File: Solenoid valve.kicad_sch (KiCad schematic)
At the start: 21 parts, among them J2 Conn_01x02, J3 Conn_01x02, J4 Conn_01x02, Q1 S8050, Q2 S8050, U1 BTS443P

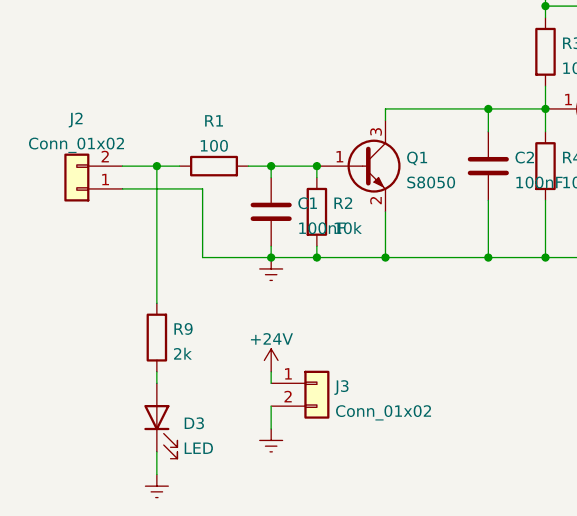
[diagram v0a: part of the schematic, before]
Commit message: Delete a LED
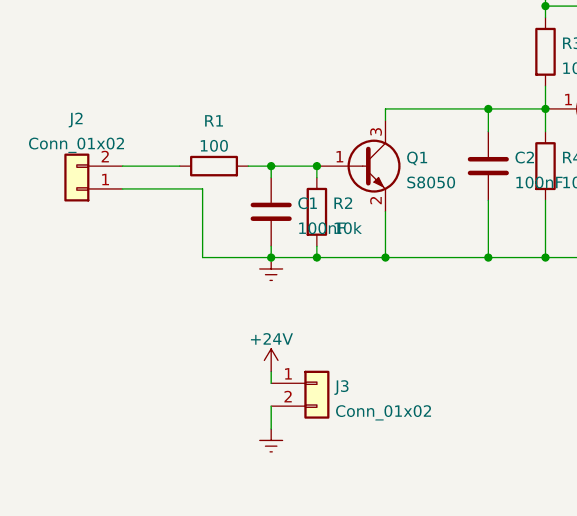
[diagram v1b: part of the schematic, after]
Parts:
- removed D3: LED, LED_SMD:LED_0603_1608Metric_Pad1.05x0.95mm_HandSolder, symbol Device:LED
- removed R9: 2k, Resistor_SMD:R_0603_1608Metric_Pad0.98x0.95mm_HandSolder, symbol Device:R
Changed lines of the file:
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@@
   (junction (at 176.53 66.04) (diameter 0) (color 0 0 0 0)
   )
-  (junction (at 90.17 76.2) (diameter 0) (color 0 0 0 0)
-  )
   (junction (at 127 69.85) (diameter 0) (color 0 0 0 0)
   )
@@
     (stroke (width 0) (type default) (color 0 0 0 0))
   )
-  (wire (pts (xy 86.36 76.2) (xy 90.17 76.2))
+  (wire (pts (xy 86.36 76.2) (xy 92.71 76.2))
     (stroke (width 0) (type default) (color 0 0 0 0))
   )
@@
     (stroke (width 0) (type default) (color 0 0 0 0))
   )
-  (wire (pts (xy 90.17 110.49) (xy 90.17 107.95))
-    (stroke (width 0) (type default) (color 0 0 0 0))
-  )
   (wire (pts (xy 102.87 77.47) (xy 102.87 76.2))
     (stroke (width 0) (type default) (color 0 0 0 0))
@@
     (stroke (width 0) (type default) (color 0 0 0 0))
   )
-  (wire (pts (xy 90.17 76.2) (xy 90.17 91.44))
-    (stroke (width 0) (type default) (color 0 0 0 0))
-  )
   (wire (pts (xy 133.35 86.36) (xy 127 86.36))
     (stroke (width 0) (type default) (color 0 0 0 0))
@@
     (stroke (width 0) (type default) (color 0 0 0 0))
   )
-  (wire (pts (xy 90.17 76.2) (xy 92.71 76.2))
-    (stroke (width 0) (type default) (color 0 0 0 0))
-  )
   (wire (pts (xy 102.87 86.36) (xy 107.95 86.36))
     (stroke (width 0) (type default) (color 0 0 0 0))
@@
   )
   (wire (pts (xy 133.35 55.88) (xy 133.35 58.42))
-    (stroke (width 0) (type default) (color 0 0 0 0))
-  )
-  (wire (pts (xy 90.17 99.06) (xy 90.17 100.33))
     (stroke (width 0) (type default) (color 0 0 0 0))
   )
@@
     (pin "1")
   )
-  (symbol (lib_id "Device:LED") (at 90.17 104.14 90) (unit 1)
-    (in_bom yes) (on_board yes) (fields_autoplaced)
-    (property "Reference" "D3" (id 0) (at 93.091 104.819 90)
-      (effects (font (size 1.27 1.27)) (justify right))
-    )
-    (property "Value" "LED" (id 1) (at 93.091 107.5941 90)
-      (effects (font (size 1.27 1.27)) (justify right))
-    )
-    (property "Footprint" "LED_SMD:LED_0603_1608Metric_Pad1.05x0.95mm_HandSolder" (id 2) (at 90.17 104.14 0)
-      (effects (font (size 1.27 1.27)) hide)
-    )
-    (property "Datasheet" "~" (id 3) (at 90.17 104.14 0)
-      (effects (font (size 1.27 1.27)) hide)
-    )
-    (pin "1")
-    (pin "2")
-  )
   (symbol (lib_id "Device:R") (at 176.53 71.12 180) (unit 1)
     (in_bom yes) (on_board yes) (fields_autoplaced)
@@
     )
     (property "Datasheet" "~" (id 3) (at 107.95 81.28 0)
-      (effects (font (size 1.27 1.27)) hide)
-    )
-    (pin "1")
-    (pin "2")
-  )
-  (symbol (lib_id "Device:R") (at 90.17 95.25 180) (unit 1)
-    (in_bom yes) (on_board yes) (fields_autoplaced)
-    (property "Reference" "R9" (id 0) (at 91.948 94.3415 0)
-      (effects (font (size 1.27 1.27)) (justify right))
-    )
-    (property "Value" "2k" (id 1) (at 91.948 97.1166 0)
-      (effects (font (size 1.27 1.27)) (justify right))
-    )
-    (property "Footprint" "Resistor_SMD:R_0603_1608Metric_Pad0.98x0.95mm_HandSolder" (id 2) (at 91.948 95.25 90)
-      (effects (font (size 1.27 1.27)) hide)
-    )
-    (property "Datasheet" "~" (id 3) (at 90.17 95.25 0)
       (effects (font (size 1.27 1.27)) hide)
     )
@@
     (pin "1")
   )
-  (symbol (lib_id "power:Earth") (at 90.17 110.49 0) (unit 1)
-    (in_bom yes) (on_board yes) (fields_autoplaced)
-    (property "Reference" "#PWR07" (id 0) (at 90.17 116.84 0)
-      (effects (font (size 1.27 1.27)) hide)
-    )
-    (property "Value" "Earth" (id 1) (at 90.17 114.3 0)
-      (effects (font (size 1.27 1.27)) hide)
-    )
-    (property "Footprint" "" (id 2) (at 90.17 110.49 0)
-      (effects (font (size 1.27 1.27)) hide)
-    )
-    (property "Datasheet" "~" (id 3) (at 90.17 110.49 0)
-      (effects (font (size 1.27 1.27)) hide)
-    )
-    (pin "1")
-  )
   (symbol (lib_id "Device:R") (at 148.59 81.28 180) (unit 1)
     (in_bom yes) (on_board yes) (fields_autoplaced)
@@
       (reference "#PWR06") (unit 1) (value "+24V") (footprint "")
     )
-    (path "/ccfc5072-c1d4-4b56-adde-ef38eddaefc1"
-      (reference "#PWR07") (unit 1) (value "Earth") (footprint "")
-    )
     (path "/bac3120c-aac0-45d3-b408-67503f2e3911"
       (reference "C1") (unit 1) (value "100nF") (footprint "Capacitor_SMD:C_0603_1608Metric_Pad1.08x0.95mm_HandSolder")
@@
       (reference "D2") (unit 1) (value "LED") (footprint "LED_SMD:LED_0603_1608Metric_Pad1.05x0.95mm_HandSolder")
     )
-    (path "/3a5c61ce-d752-42bb-b21f-ed0b26288b02"
-      (reference "D3") (unit 1) (value "LED") (footprint "LED_SMD:LED_0603_1608Metric_Pad1.05x0.95mm_HandSolder")
-    )
     (path "/bc6fce76-cd5f-4a02-afb0-06d97d829d77"
       (reference "J2") (unit 1) (value "Conn_01x02") (footprint "Connector_JST:JST_GH_SM02B-GHS-TB_1x02-1MP_P1.25mm_Horizontal")
@@
       (reference "R8") (unit 1) (value "10k") (footprint "Resistor_SMD:R_0603_1608Metric_Pad0.98x0.95mm_HandSolder")
     )
-    (path "/5d29185e-00f9-4ea8-a9a9-589fda3ba20a"
-      (reference "R9") (unit 1) (value "2k") (footprint "Resistor_SMD:R_0603_1608Metric_Pad0.98x0.95mm_HandSolder")
-    )
     (path "/fc95094a-b02a-4ae0-800c-e6c89c3d2f0e"
